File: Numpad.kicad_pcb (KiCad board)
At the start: 2 copper layers, 82.6 x 127 mm, 68 parts, among them J1 SWD, J2 USB_C_Receptacle_USB2.0, U1 SRV05-4, U2 STM32F103C8Tx, U3 XC6206PxxxMR, Y1 8MHz

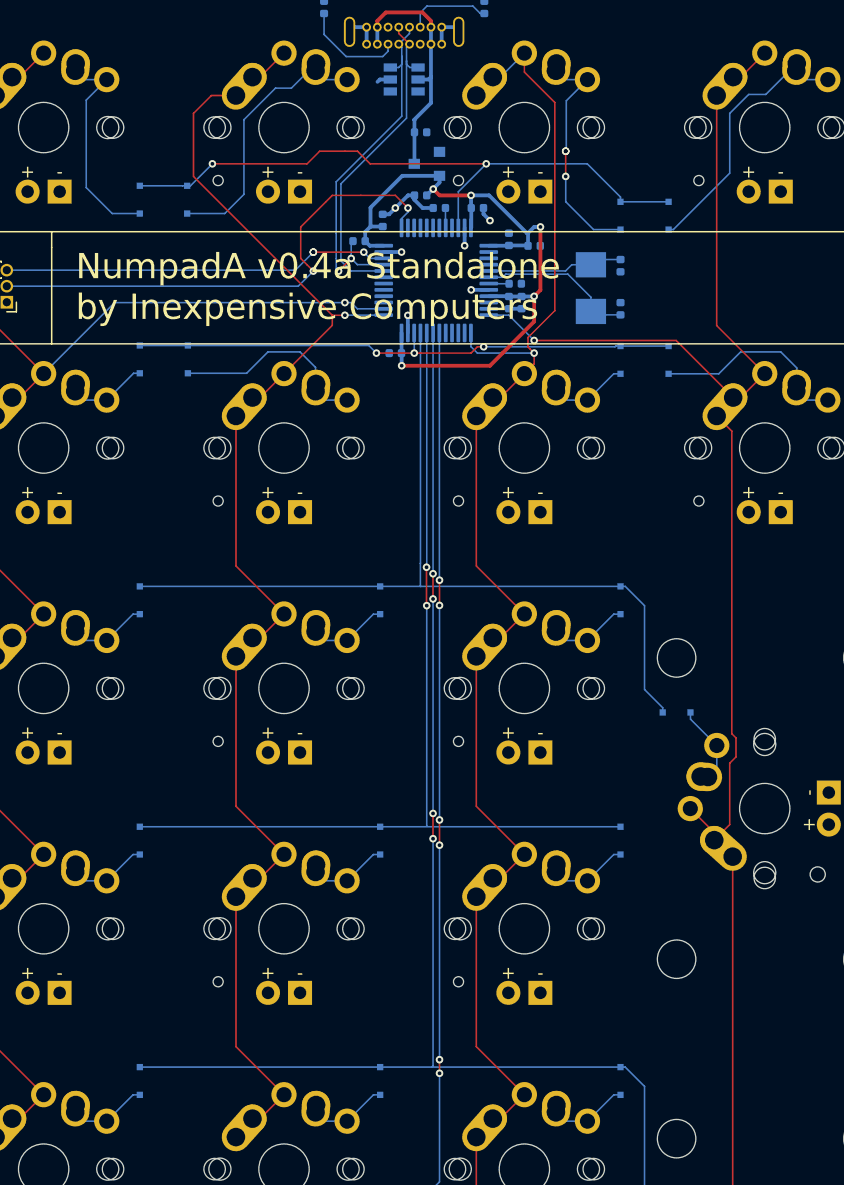
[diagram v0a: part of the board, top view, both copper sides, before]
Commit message: Fixed positioning of silkscreen labels
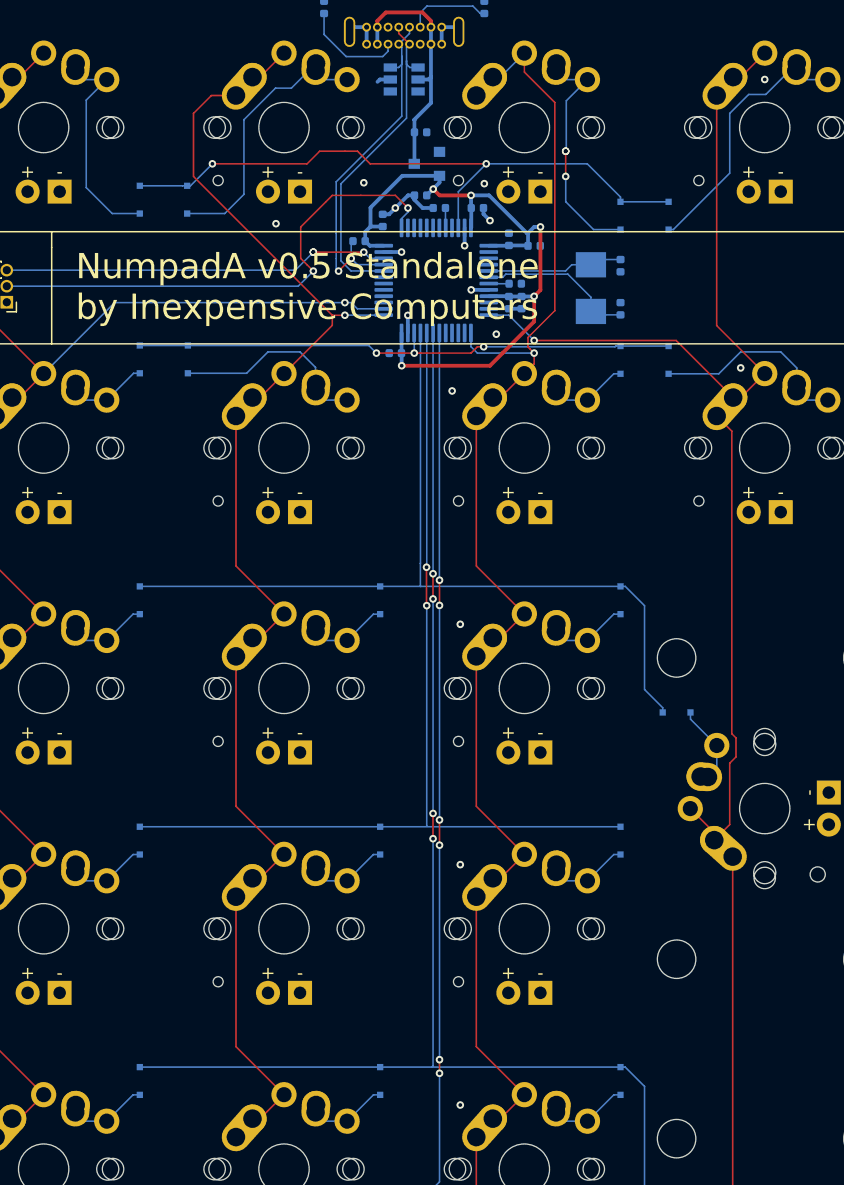
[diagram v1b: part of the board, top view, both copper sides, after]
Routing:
- net GND: vias 6 -> 16
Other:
- board text added: "NumpadA v0.5 Standalone by Inexpensive Computers"
- board text removed: "NumpadA v0.4a Standalone by Inexpensive Computers"
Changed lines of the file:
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@@
     (thickness 1.6)
     (drawings 16)
-    (tracks 511)
+    (tracks 521)
     (zones 0)
     (modules 68)
@@
     (last_trace_width 0.127)
     (trace_clearance 0.127)
-    (zone_clearance 0.508)
+    (zone_clearance 0.254)
     (zone_45_only yes)
     (trace_min 0.127)
@@
     (tags SOD-323F)
     (attr smd)
-    (fp_text reference D_TAB1 (at 0 1.85 90) (layer B.SilkS)
+    (fp_text reference D_TAB1 (at 0 -1.5 90) (layer B.SilkS)
       (effects (font (size 1 1) (thickness 0.15)) (justify mirror))
     )
@@
     (tags SOD-323F)
     (attr smd)
-    (fp_text reference D_STAR1 (at 0 1.85 90) (layer B.SilkS)
+    (fp_text reference D_STAR1 (at -0.04 -1.655 90) (layer B.SilkS)
       (effects (font (size 1 1) (thickness 0.15)) (justify mirror))
     )
@@
     (tags SOD-323F)
     (attr smd)
-    (fp_text reference D_SLASH1 (at 0 1.85 90) (layer B.SilkS)
+    (fp_text reference D_SLASH1 (at 0 -1.945 90) (layer B.SilkS)
       (effects (font (size 1 1) (thickness 0.15)) (justify mirror))
     )
@@
     (tags SOD-323F)
     (attr smd)
-    (fp_text reference D_PLUS1 (at 0 1.85) (layer B.SilkS)
+    (fp_text reference D_PLUS1 (at 0 -1.48) (layer B.SilkS)
       (effects (font (size 1 1) (thickness 0.15)) (justify mirror))
     )
@@
     (tags SOD-323F)
     (attr smd)
-    (fp_text reference D_NUMLK1 (at 0 1.85 90) (layer B.SilkS)
+    (fp_text reference D_NUMLK1 (at 0 -1.755 90) (layer B.SilkS)
       (effects (font (size 1 1) (thickness 0.15)) (justify mirror))
     )
@@
     (tags SOD-323F)
     (attr smd)
-    (fp_text reference D_MINUS1 (at 0 1.85 90) (layer B.SilkS)
+    (fp_text reference D_MINUS1 (at 0 -1.845 90) (layer B.SilkS)
       (effects (font (size 1 1) (thickness 0.15)) (justify mirror))
     )
@@
     (tags SOD-323F)
     (attr smd)
-    (fp_text reference D_FN1 (at 0 1.85 90) (layer B.SilkS)
+    (fp_text reference D_FN1 (at 0 -1.655 90) (layer B.SilkS)
       (effects (font (size 1 1) (thickness 0.15)) (justify mirror))
     )
@@
     (tags SOD-323F)
     (attr smd)
-    (fp_text reference D_ESC1 (at 0 1.85 90) (layer B.SilkS)
+    (fp_text reference D_ESC1 (at 0 -1.755 90) (layer B.SilkS)
       (effects (font (size 1 1) (thickness 0.15)) (justify mirror))
     )
@@
     (tags SOD-323F)
     (attr smd)
-    (fp_text reference D_ENTER1 (at 0 1.85) (layer B.SilkS)
+    (fp_text reference D_ENTER1 (at 0 -1.85) (layer B.SilkS)
       (effects (font (size 1 1) (thickness 0.15)) (justify mirror))
     )
@@
     (tags SOD-323F)
     (attr smd)
-    (fp_text reference D_DOT1 (at 0 1.85 90) (layer B.SilkS)
+    (fp_text reference D_DOT1 (at 0 -2.155 90) (layer B.SilkS)
       (effects (font (size 1 1) (thickness 0.15)) (justify mirror))
     )
@@
     (tags SOD-323F)
     (attr smd)
-    (fp_text reference D_BKSP1 (at 0 1.85 90) (layer B.SilkS)
+    (fp_text reference D_BKSP1 (at 0 -1.845 90) (layer B.SilkS)
       (effects (font (size 1 1) (thickness 0.15)) (justify mirror))
     )
@@
     (tags SOD-323F)
     (attr smd)
-    (fp_text reference D_0 (at 0 1.85 90) (layer B.SilkS)
+    (fp_text reference D_0 (at 0 1.77 90) (layer B.SilkS)
       (effects (font (size 1 1) (thickness 0.15)) (justify mirror))
     )
@@
     (tags resistor)
     (attr smd)
-    (fp_text reference R1 (at -1.015 1) (layer B.SilkS)
+    (fp_text reference R1 (at -0.515 1) (layer B.SilkS)
       (effects (font (size 1 1) (thickness 0.15)) (justify mirror))
     )
@@
   (gr_arc (start 177.8 38.1) (end 180.975 38.1) (angle -90) (layer Edge.Cuts) (width 0.12))
   (gr_line (start 180.975 44.45) (end 180.975 38.1) (layer Edge.Cuts) (width 0.05))
-  (gr_text "NumpadA v0.4a Standalone\nby Inexpensive Computers" (at 113.665 60.25) (layer F.SilkS)
+  (gr_text "NumpadA v0.5 Standalone\nby Inexpensive Computers" (at 113.665 60.25) (layer F.SilkS)
     (effects (font (size 2 2) (thickness 0.15)) (justify left))
   )
@@
   (segment (start 145.985 54) (end 145.985 54.485) (width 0.3) (layer B.Cu) (net 11))
   (segment (start 145.985 54.485) (end 146.5 55) (width 0.3) (layer B.Cu) (net 11))
+  (via (at 129.54 55.245) (size 0.6) (drill 0.3) (layers F.Cu B.Cu) (net 11))
+  (via (at 144.145 86.995) (size 0.6) (drill 0.3) (layers F.Cu B.Cu) (net 11))
+  (via (at 144.145 125.095) (size 0.6) (drill 0.3) (layers F.Cu B.Cu) (net 11))
+  (via (at 144.145 106.045) (size 0.6) (drill 0.3) (layers F.Cu B.Cu) (net 11))
+  (via (at 166.37 66.675) (size 0.6) (drill 0.3) (layers F.Cu B.Cu) (net 11))
+  (via (at 168.275 43.815) (size 0.6) (drill 0.3) (layers F.Cu B.Cu) (net 11))
+  (via (at 146.05 52.07) (size 0.6) (drill 0.3) (layers F.Cu B.Cu) (net 11))
+  (via (at 136.5 52) (size 0.6) (drill 0.3) (layers F.Cu B.Cu) (net 11))
+  (via (at 143.5 68.5) (size 0.6) (drill 0.3) (layers F.Cu B.Cu) (net 11))
+  (via (at 147 64) (size 0.6) (drill 0.3) (layers F.Cu B.Cu) (net 11))
   (segment (start 141.82164 39.66718) (end 141.82164 41.01718) (width 0.3) (layer B.Cu) (net 12))
   (segment (start 137.57164 39.66718) (end 137.57164 41.01718) (width 0.3) (layer B.Cu) (net 12))
@@
   (segment (start 142.97 54) (end 142.97 55.5575) (width 0.127) (layer B.Cu) (net 44))
   (zone (net 11) (net_name GND) (layer F.Cu) (hatch edge 0.508)
-    (connect_pads yes (clearance 0.508))
-    (min_thickness 0.254)
+    (connect_pads yes (clearance 0.254))
+    (min_thickness 0.127)
     (fill yes (arc_segments 32) (thermal_gap 0.508) (thermal_bridge_width 0.508) (smoothing fillet) (radius 3.175))
     (polygon
@@
   )
   (zone (net 11) (net_name GND) (layer B.Cu) (hatch edge 0.508)
-    (connect_pads yes (clearance 0.508))
-    (min_thickness 0.254)
+    (connect_pads yes (clearance 0.254))
+    (min_thickness 0.127)
     (fill yes (arc_segments 32) (thermal_gap 0.508) (thermal_bridge_width 0.508) (smoothing fillet) (radius 3.175))
     (polygon

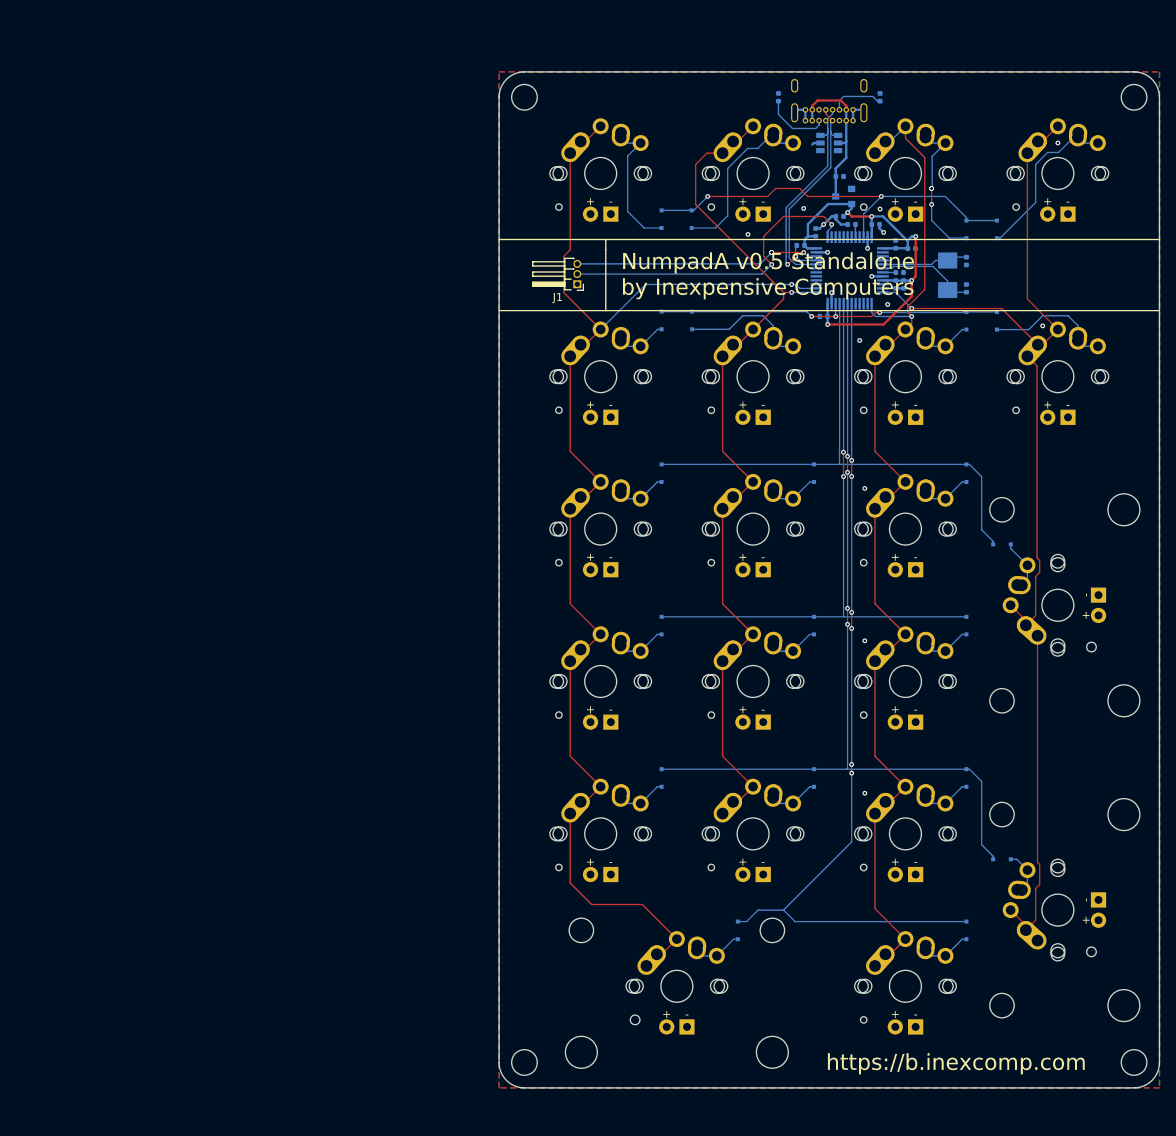
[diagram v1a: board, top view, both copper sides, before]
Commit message: Updated PCB sheet details
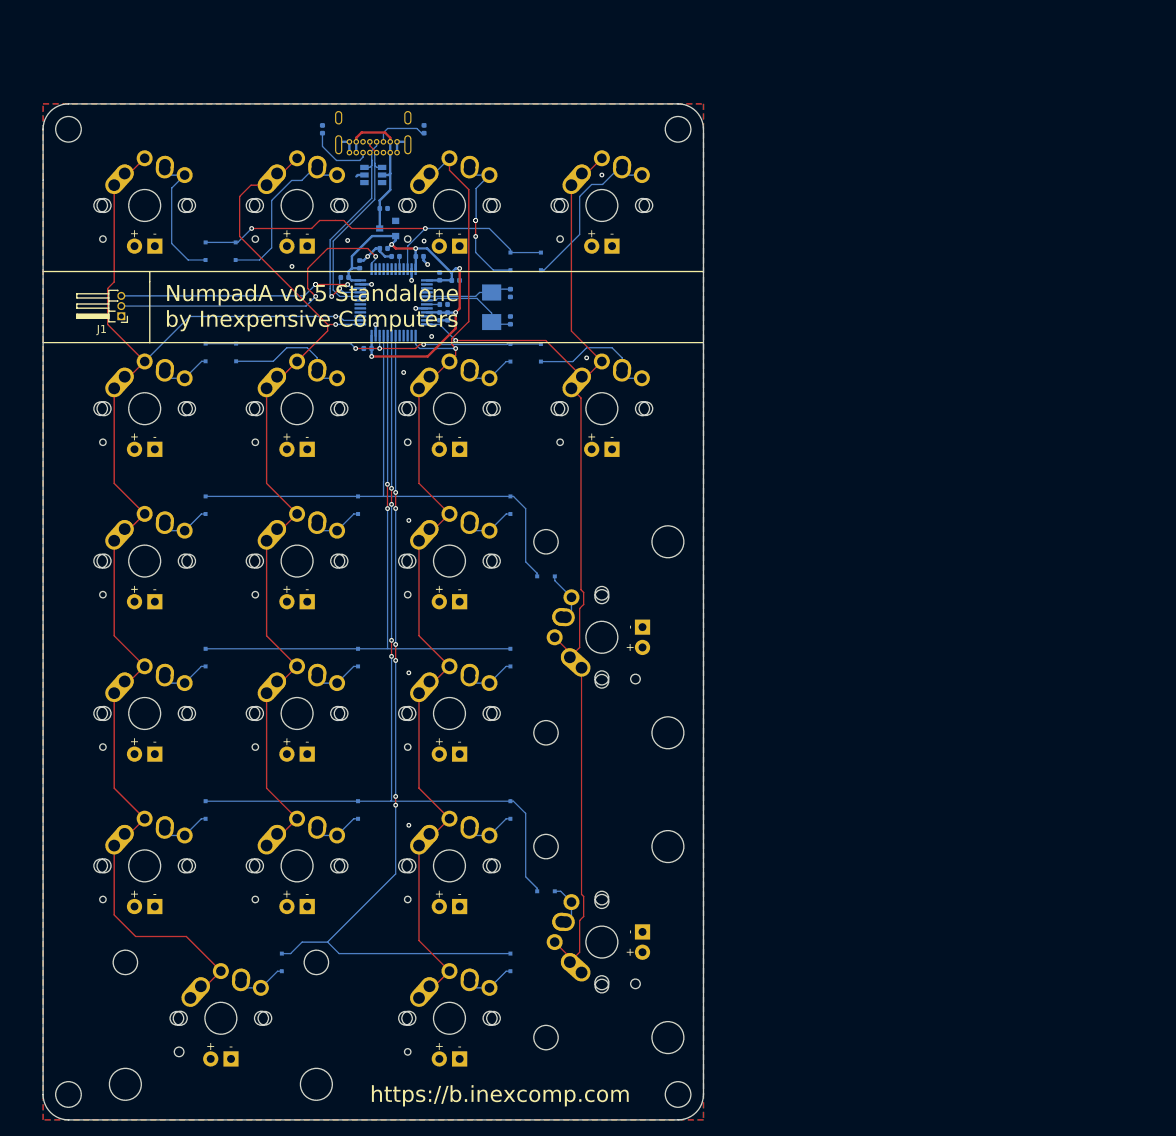
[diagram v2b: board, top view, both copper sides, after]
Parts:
- moved D_0 57.1 mm to (71.3, 146.2)
- moved H2 57.1 mm to (120.8, 42.1)
- moved H4 57.1 mm to (120.8, 162.8)
- moved J2 57.1 mm to (79.7, 45.0)
- moved R1 57.1 mm to (85.5, 58.0)
- moved R3 57.1 mm to (89.0, 42.1)
- moved SW_2 57.1 mm to (73.2, 134.2)
- moved SW_5 57.1 mm to (73.2, 115.1)
- moved SW_8 57.1 mm to (73.2, 96.1)
- moved SW_SLASH1 57.1 mm to (73.2, 77.0)
- moved SW_TAB1 57.1 mm to (73.2, 51.6)
- moved U2 57.1 mm to (85.2, 63.7)
- moved D_1 57.1 mm to (61.7, 127.2)
- moved D_4 57.1 mm to (61.7, 108.1)
- moved D_7 57.1 mm to (61.7, 89.1)
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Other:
- outline, holes or cut-outs redrawn

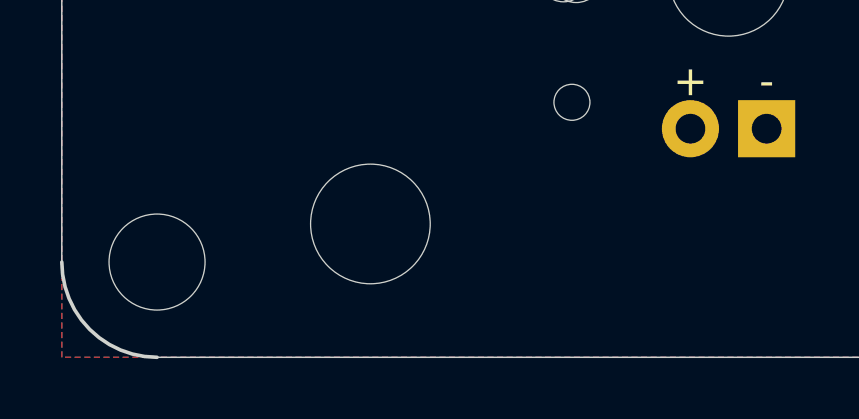
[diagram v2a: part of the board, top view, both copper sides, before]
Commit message: Added place for JLCPCB order number
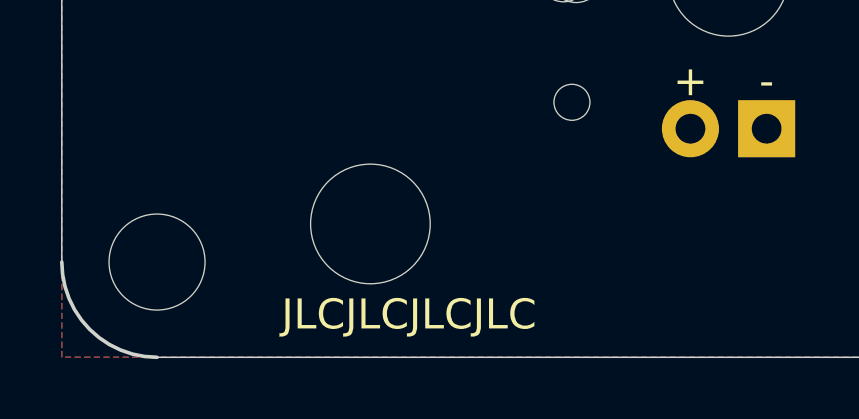
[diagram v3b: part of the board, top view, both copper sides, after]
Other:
- board text added: "JLCJLCJLCJLC"
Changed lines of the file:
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@@
   (general
     (thickness 1.6)
-    (drawings 16)
+    (drawings 17)
     (tracks 521)
     (zones 0)
@@
       (drillshape 0)
       (scaleselection 1)
-      (outputdirectory "./gerber"))
+      (outputdirectory "/home/dmitry/Documents/NumpadA/gerber/"))
   )
   (net 0 "")
@@
     )
   )
+  (gr_text JLCJLCJLCJLC (at 53 164.5) (layer F.SilkS)
+    (effects (font (size 1 1) (thickness 0.2)))
+  )
   (gr_text https://b.inexcomp.com (at 98.575 162.75) (layer F.SilkS)
